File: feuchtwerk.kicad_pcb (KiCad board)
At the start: 2 copper layers, 30.5 x 38.2 mm, 47 parts, among them P1 CONN_01X04, P2 CONN_01X08, P3 CONN_01X08, U1 STM32F042K6Tx, U2 HDC1080, U3 MCP1754ST-3302E/MB, U4 MCP1754ST-5002E/MB, U5 TJA1051/3, X1 CON_SWD, Y1 8MHz

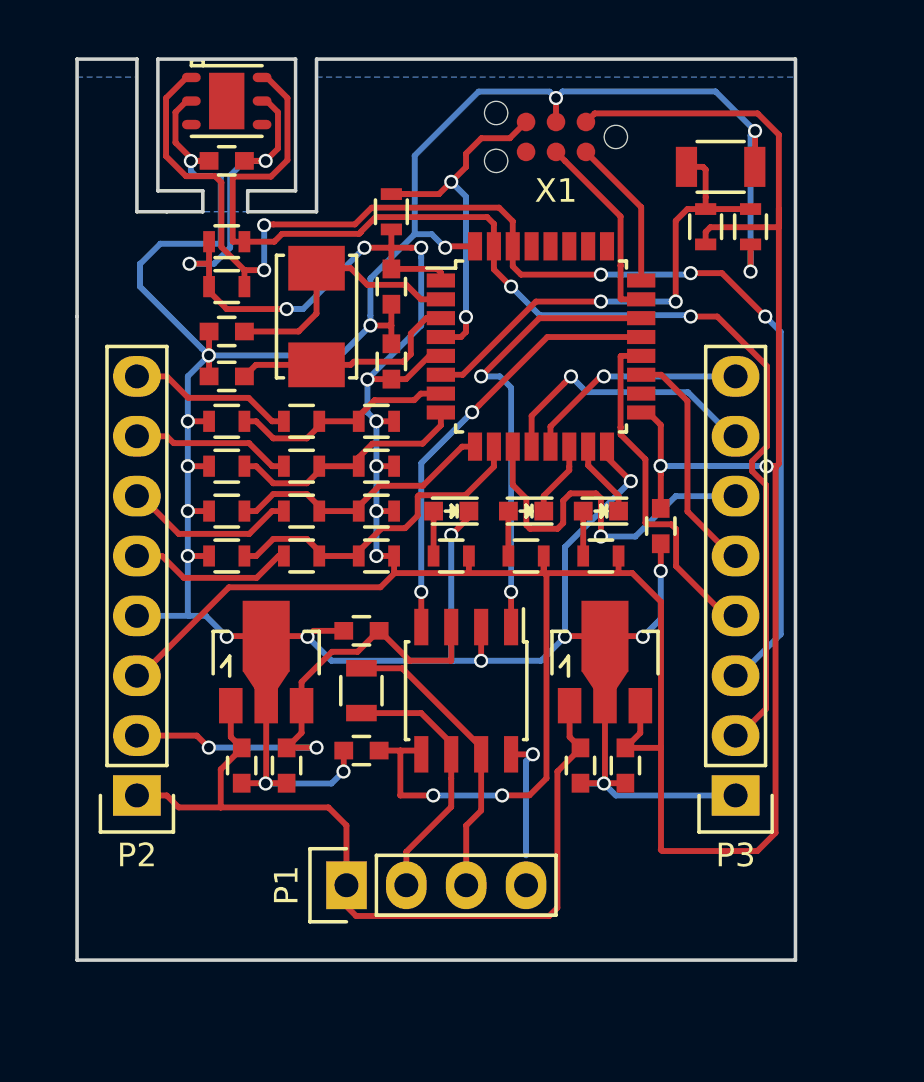
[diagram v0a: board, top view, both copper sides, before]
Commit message: change board dimensions, milling slot for humidity sensor
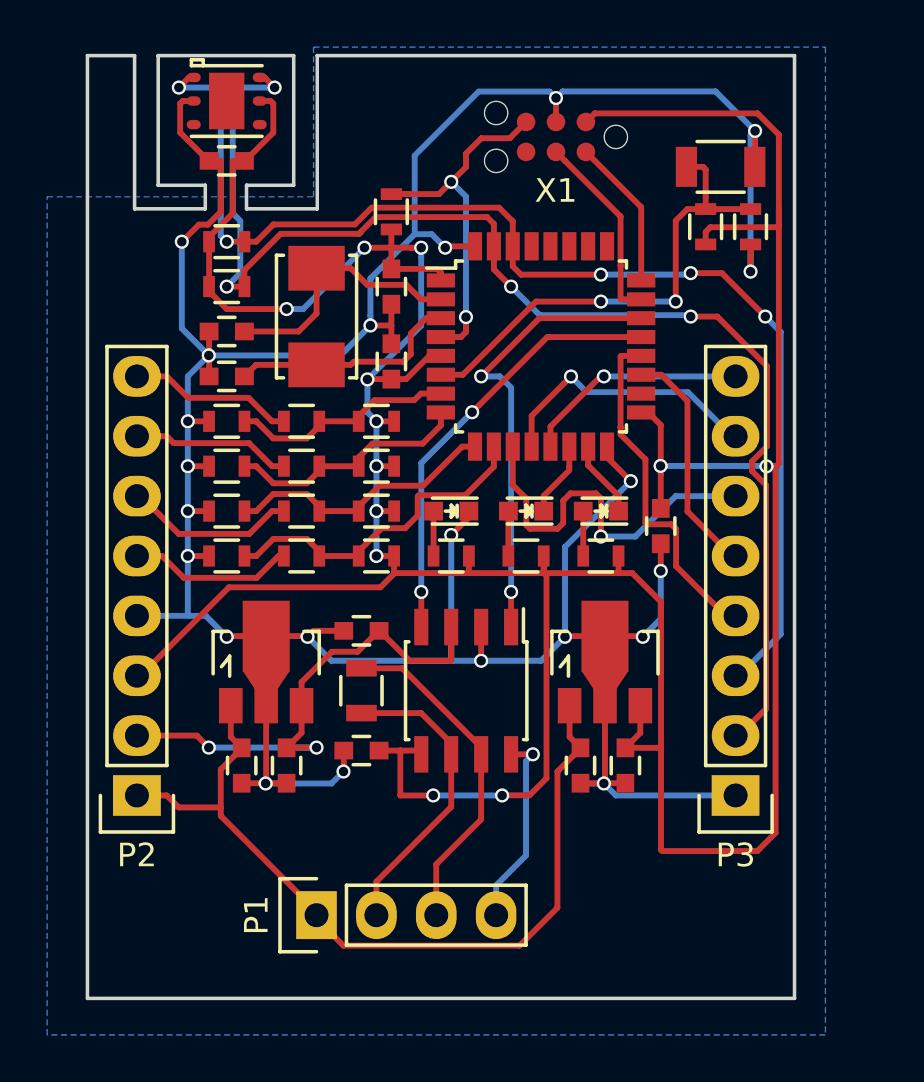
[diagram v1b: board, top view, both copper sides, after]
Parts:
- moved R14 1.91 mm to (105.4, 112.4)
- moved R17 1.91 mm to (105.4, 114.3)
- moved P1 1.80 mm to (109.2, 141.0)
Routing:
- net +3V3: track 169.2 -> 165.3 mm, vias 14 -> 12
- net SCL: track 53.1 -> 56.5 mm, vias 2 -> 4
- net SDA: track 55.3 -> 52.3 mm
- net CAN_H: track 12.6 -> 14.4 mm
- net CAN_L: track 11.3 -> 13.0 mm
- net GND: track 163.7 -> 162.2 mm
- net VCC: track 36.2 -> 35.6 mm
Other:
- board size 30.5 x 38.2 mm -> 30 x 40 mm

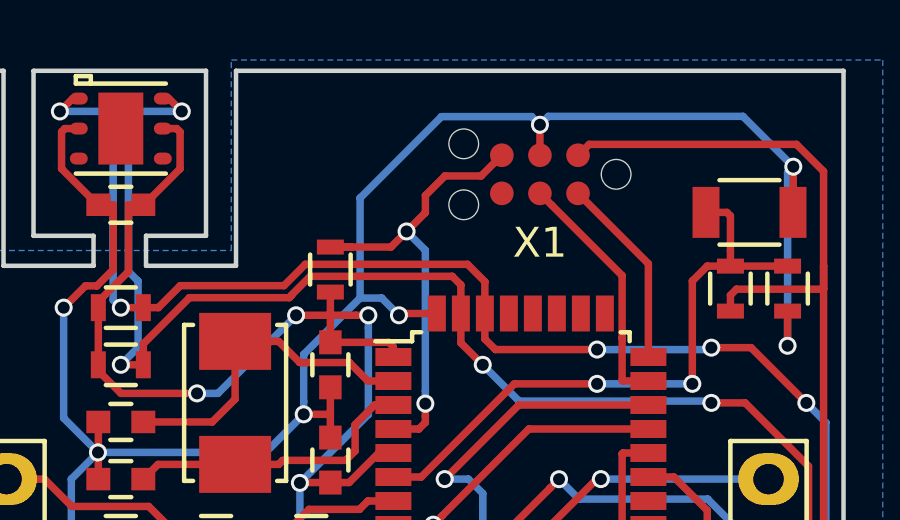
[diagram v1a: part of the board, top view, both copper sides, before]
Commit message: add clearance around tagconnect drills
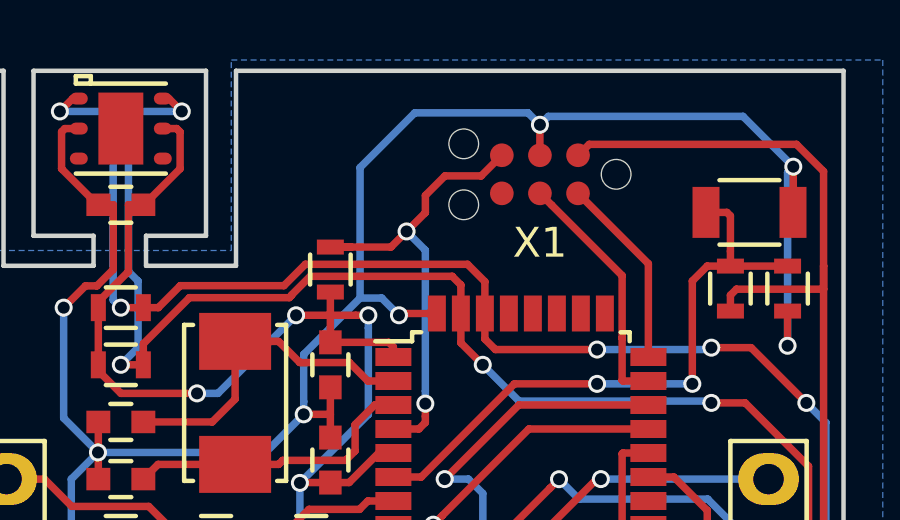
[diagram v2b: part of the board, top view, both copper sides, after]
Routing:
- net GND: track 162.2 -> 162.9 mm
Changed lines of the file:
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@@
     (mod_text_size 1 1)
     (mod_text_width 0.15)
-    (pad_size 1.524 1.524)
-    (pad_drill 0.762)
+    (pad_size 0.9906 0.9906)
+    (pad_drill 0.9906)
     (pad_to_mask_clearance 0.05)
     (aux_axis_origin 0 0)
@@
       (effects (font (size 1 1) (thickness 0.15)))
     )
-    (pad "" np_thru_hole circle (at 2.54 -1.016 180) (size 0.9906 0.9906) (drill 0.9906) (layers *.Cu *.Mask F.SilkS))
-    (pad "" np_thru_hole circle (at 2.54 1.016 180) (size 0.9906 0.9906) (drill 0.9906) (layers *.Cu *.Mask F.SilkS))
+    (pad "" np_thru_hole circle (at 2.54 -1.016 180) (size 0.9906 0.9906) (drill 0.9906) (layers *.Cu *.Mask F.SilkS)
+      (clearance 0.3))
+    (pad "" np_thru_hole circle (at 2.54 1.016 180) (size 0.9906 0.9906) (drill 0.9906) (layers *.Cu *.Mask F.SilkS)
+      (clearance 0.3))
     (pad 5 connect circle (at 1.27 0.635 180) (size 0.7874 0.7874) (layers F.Cu F.Mask)
       (net 21 NRST))
@@
     (pad 4 connect circle (at 0 -0.635 180) (size 0.7874 0.7874) (layers F.Cu F.Mask)
       (net 28 SWDIO))
-    (pad "" np_thru_hole circle (at -2.54 0 180) (size 0.9906 0.9906) (drill 0.9906) (layers *.Cu *.Mask F.SilkS))
+    (pad "" np_thru_hole circle (at -2.54 0 180) (size 0.9906 0.9906) (drill 0.9906) (layers *.Cu *.Mask F.SilkS)
+      (clearance 0.3))
   )
   (module Crystals:ABM3 (layer F.Cu)
@@
   (segment (start 122.995 114.04) (end 122.995 110.93) (width 0.25) (layer F.Cu) (net 29))
   (segment (start 122.995 110.93) (end 120.65 108.585) (width 0.25) (layer F.Cu) (net 29))
+  (segment (start 119.38 106.299) (end 118.982715 105.901715) (width 0.25) (layer B.Cu) (net 30))
+  (segment (start 113.384829 107.725982) (end 113.384829 112.074351) (width 0.25) (layer B.Cu) (net 30))
+  (segment (start 118.982715 105.901715) (end 115.209096 105.901715) (width 0.25) (layer B.Cu) (net 30))
+  (segment (start 115.209096 105.901715) (end 113.384829 107.725982) (width 0.25) (layer B.Cu) (net 30))
   (segment (start 118.11 138.43) (end 116.84 139.7) (width 0.25) (layer B.Cu) (net 30))
   (segment (start 116.84 139.7) (end 116.84 140.97) (width 0.25) (layer B.Cu) (net 30))
@@
   (segment (start 119.6601 106.0189) (end 126.1484 106.0189) (width 0.25) (layer B.Cu) (net 30))
   (segment (start 126.1484 106.0189) (end 127.8255 107.696) (width 0.25) (layer B.Cu) (net 30))
-  (segment (start 119.38 106.299) (end 119.107162 106.026162) (width 0.25) (layer B.Cu) (net 30))
-  (segment (start 119.107162 106.026162) (end 116.101121 106.026162) (width 0.25) (layer B.Cu) (net 30))
-  (segment (start 116.101121 106.026162) (end 113.384829 108.742454) (width 0.25) (layer B.Cu) (net 30))
-  (segment (start 113.384829 108.742454) (end 113.384829 112.074351) (width 0.25) (layer B.Cu) (net 30))
   (segment (start 127.635 113.665) (end 127.635 107.8865) (width 0.25) (layer B.Cu) (net 30))
   (segment (start 127.635 107.8865) (end 127.8255 107.696) (width 0.25) (layer B.Cu) (net 30))

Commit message: add fiducials
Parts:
- added REF**: Fiducial_1mm_Dia_2.54mm_Outer_CopperTop, Fiducials:Fiducial_1mm_Dia_2.54mm_Outer_CopperTop, F.Cu at (127.0, 142.0)
- added REF**: Fiducial_1mm_Dia_2.54mm_Outer_CopperTop, Fiducials:Fiducial_1mm_Dia_2.54mm_Outer_CopperTop, F.Cu at (111.5, 107.0)
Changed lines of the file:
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@@
 (kicad_pcb (version 4) (host pcbnew 4.0.2+dfsg1-stable)
   (general
-    (links 115)
+    (links 0)
     (no_connects 0)
     (area 99.424999 104.424999 129.575001 144.575001)
@@
     (tracks 571)
     (zones 0)
-    (modules 47)
+    (modules 49)
     (nets 35)
   )
@@
       (outputformat 1)
       (mirror false)
-      (drillshape 1)
+      (drillshape 0)
       (scaleselection 1)
-      (outputdirectory ""))
+      (outputdirectory export/v1.0/))
   )
   (net 0 "")
@@
     (add_net VCC)
   )
+  (module Fiducials:Fiducial_1mm_Dia_2.54mm_Outer_CopperTop (layer F.Cu)
+    (at 127 142)
+    (descr "Circular Fiducial, 1mm bare copper top; 2.54mm keepout")
+    (tags marker)
+    (attr virtual)
+    (fp_text reference REF** (at 3.4 0.7) (layer F.SilkS)
+      (effects (font (size 1 1) (thickness 0.15)))
+    )
+    (fp_text value Fiducial_1mm_Dia_2.54mm_Outer_CopperTop (at 0 -1.8) (layer F.Fab)
+      (effects (font (size 1 1) (thickness 0.15)))
+    )
+    (fp_circle (center 0 0) (end 1.55 0) (layer F.CrtYd) (width 0.05))
+    (pad ~ smd circle (at 0 0) (size 1 1) (layers F.Cu F.Mask)
+      (solder_mask_margin 0.77) (clearance 0.77))
+  )
   (module Resistors_SMD:R_0603 (layer F.Cu)
     (at 105.41 112.395)
@@
     )
   )
+  (module Fiducials:Fiducial_1mm_Dia_2.54mm_Outer_CopperTop (layer F.Cu)
+    (at 111.5 107)
+    (descr "Circular Fiducial, 1mm bare copper top; 2.54mm keepout")
+    (tags marker)
+    (attr virtual)
+    (fp_text reference REF** (at 3.4 0.7) (layer F.SilkS)
+      (effects (font (size 1 1) (thickness 0.15)))
+    )
+    (fp_text value Fiducial_1mm_Dia_2.54mm_Outer_CopperTop (at 0 -1.8) (layer F.Fab)
+      (effects (font (size 1 1) (thickness 0.15)))
+    )
+    (fp_circle (center 0 0) (end 1.55 0) (layer F.CrtYd) (width 0.05))
+    (pad ~ smd circle (at 0 0) (size 1 1) (layers F.Cu F.Mask)
+      (solder_mask_margin 0.77) (clearance 0.77))
+  )
   (gr_line (start 129.5 144.5) (end 99.5 144.5) (layer Edge.Cuts) (width 0.15))
